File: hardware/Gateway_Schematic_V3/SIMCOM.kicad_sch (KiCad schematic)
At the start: 58 parts, among them IC2 SIM7600CE-H, J10 ANT_LTE, J11 ANT_LTE, J12 ANT_LTE, J14 SIM7100-6pin-socket-smd, Q1 MMBT3904, Q2 BC817, Q3 BC817, Q4 BC817, Q8 MMBT3904

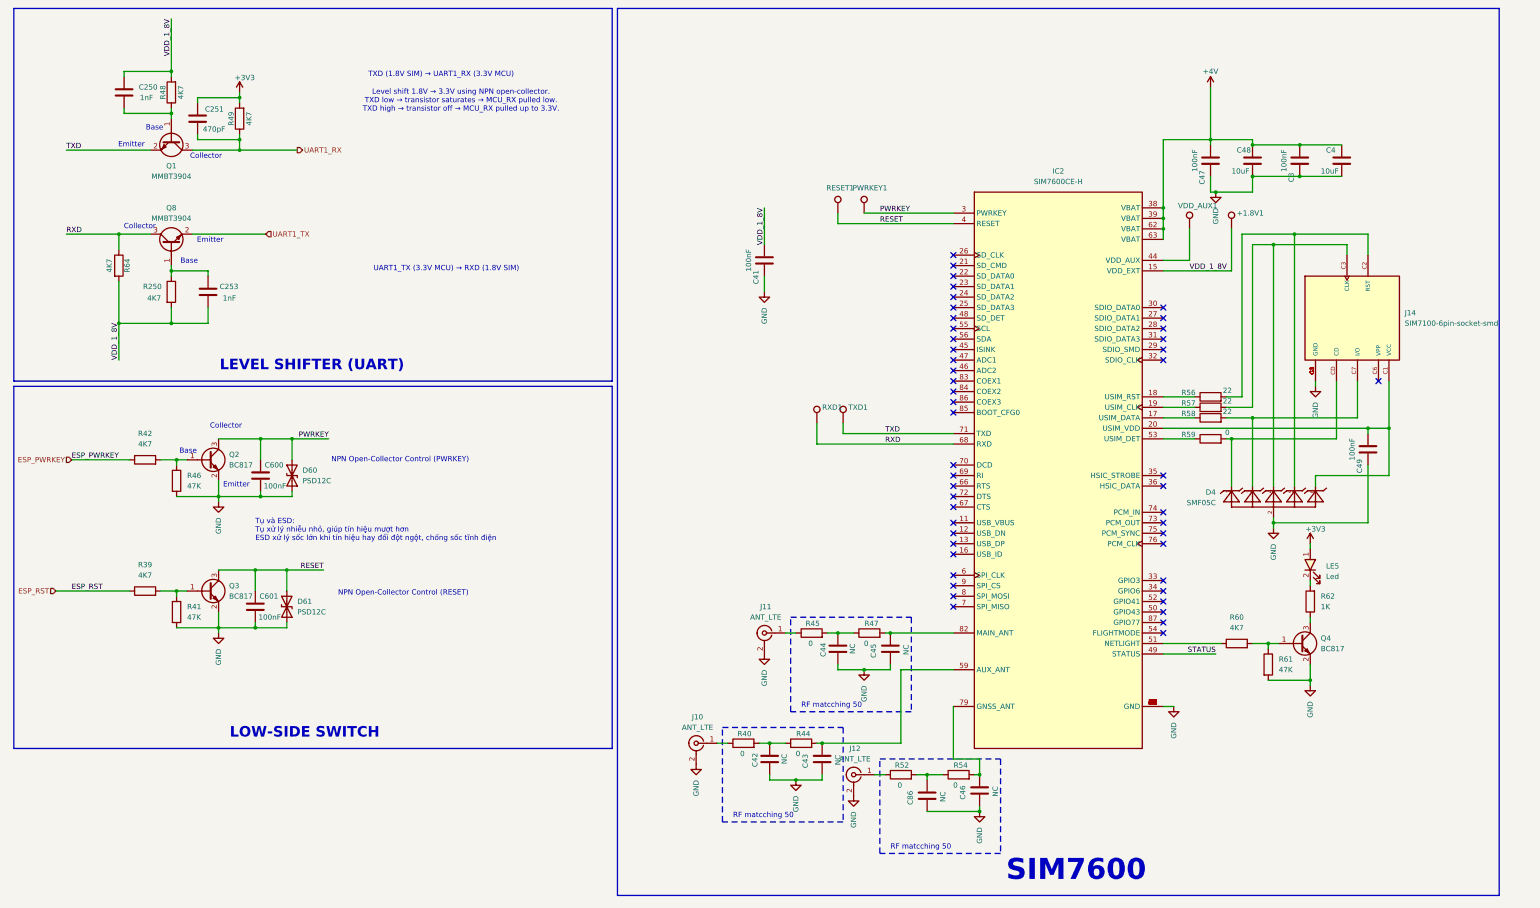
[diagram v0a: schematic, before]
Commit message: Update PCB Layout after review 27/3/2026
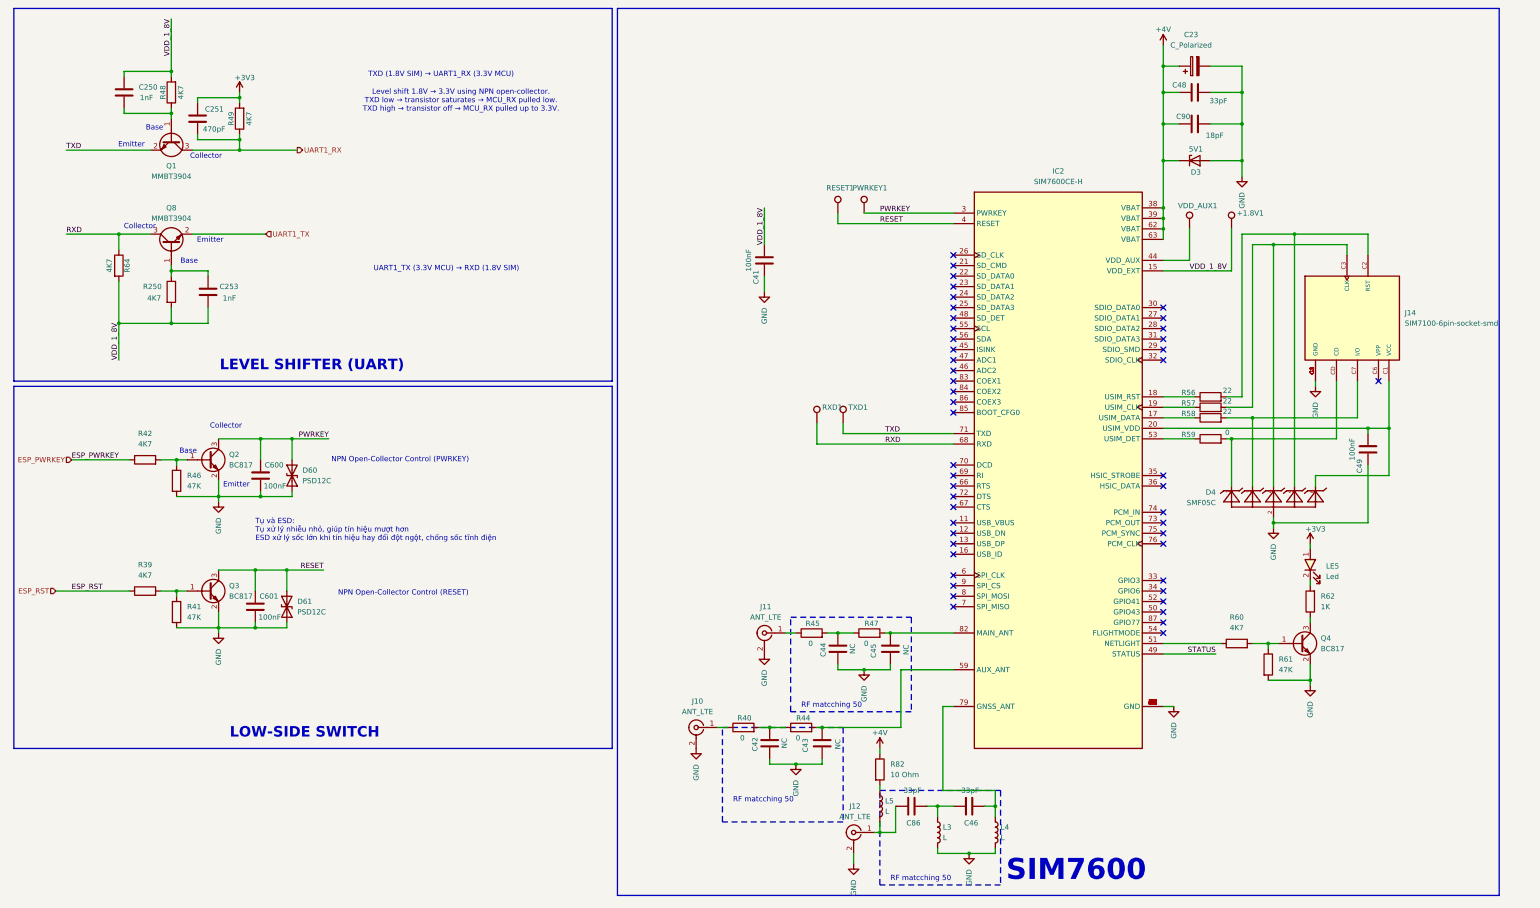
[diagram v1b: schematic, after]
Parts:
- removed C4: 10uF, Capacitor_SMD:C_0603_1608Metric, symbol Device:C
- removed C47: 100nF, Capacitor_SMD:C_0603_1608Metric, symbol Device:C
- removed R52, R54: 0, Resistor_SMD:R_0603_1608Metric, symbol Device:R
- added C23: C_Polarized, IVS_NEW_FOOTPRINT:CP_Elec_6.3x7.7, symbol Device:C_Polarized
- added D3: 5V1, IVS_NEW_FOOTPRINT:D_SOD-123, symbol Device:D_Zener
- added L3, L4, L5: L, IVS_NEW_FOOTPRINT:L_0603_1608Metric, symbol Device:L
- added R82: 10 Ohm, IVS_NEW_FOOTPRINT:R_0603_1608Metric, symbol Device:R
- C46, C86: value NC -> 33pF
- C48: value 10uF -> 33pF
- C90: renamed from C3; value 100nF -> 18pF
- J14: footprint GATEWAY_LIB:GCT_SIM7100-6-socket-smd -> IVS_NEW_FOOTPRINT:CUI_NSIM-1-A
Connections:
- net +4V: now also C23.1, D3.1 (K), R82.1
- net GND: now also C23.2, D3.2 (A), L3.2, L4.2; no longer C46.1, C86.1
- net at J12.1 (In): now also C86.2, L5.2
- net at IC2.79 (GNSS_ANT): now also C46.1, L4.1; no longer C46.2
- new net: L5.1, R82.2
- new net: C46.2, C86.1, L3.1
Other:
- moved on the sheet: C42, C43, C46, C48, C86, C90, J10, J12, R40, R44

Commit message: Update: add L_ferrite for SIMCOM
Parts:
- added L6: L_Ferrite_Small, IVS_NEW_FOOTPRINT:L_0805, symbol Device:L_Ferrite_Small
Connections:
- net +4V: now also L6.1, L6.2
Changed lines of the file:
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@@
 	(wire
 		(pts
+			(xy 293.37 40.64) (xy 294.64 40.64)
+		)
+		(stroke
+			(width 0)
+			(type default)
+		)
+	)
+	(wire
+		(pts
 			(xy 231.14 177.8) (xy 234.95 177.8)
 		)
@@
 	(wire
 		(pts
-			(xy 309.88 35.56) (xy 309.88 40.64)
+			(xy 293.37 31.75) (xy 293.37 40.64)
 		)
 		(stroke
@@
 	(wire
 		(pts
+			(xy 299.72 40.64) (xy 309.88 40.64)
+		)
+		(stroke
+			(width 0)
+			(type default)
+		)
+	)
+	(wire
+		(pts
 			(xy 341.63 81.28) (xy 341.63 142.24)
 		)
@@
 		)
 	)
+	(label "+4V"
+		(at 303.53 40.64 0)
+		(effects
+			(font
+				(size 1.27 1.27)
+			)
+			(justify left bottom)
+		)
+	)
 	(label "RESET"
 		(at 241.3 78.74 0)
@@
 	)
 	(symbol
+		(lib_id "Device:L_Ferrite_Small")
+		(at 297.18 40.64 90)
+		(unit 1)
+		(exclude_from_sim no)
+		(in_bom yes)
+		(on_board yes)
+		(dnp no)
+		(fields_autoplaced yes)
+		(property "Reference" "L6"
+			(at 297.18 34.29 90)
+			(effects
+				(font
+					(size 1.27 1.27)
+				)
+			)
+		)
+		(property "Value" "L_Ferrite_Small"
+			(at 297.18 36.83 90)
+			(effects
+				(font
+					(size 1.27 1.27)
+				)
+			)
+		)
+		(property "Footprint" "IVS_NEW_FOOTPRINT:L_0805"
+			(at 297.18 40.64 0)
+			(effects
+				(font
+					(size 1.27 1.27)
+				)
+				(hide yes)
+			)
+		)
+		(property "Datasheet" "~"
+			(at 297.18 40.64 0)
+			(effects
+				(font
+					(size 1.27 1.27)
+				)
+				(hide yes)
+			)
+		)
+		(property "Description" "Inductor with ferrite core, small symbol"
+			(at 297.18 40.64 0)
+			(effects
+				(font
+					(size 1.27 1.27)
+				)
+				(hide yes)
+			)
+		)
+		(pin "1"
+		)
+		(pin "2"
+		)
+		(instances
+			(project "Gateway_Schematic_V3"
+				(path "/08b065f5-231d-43cb-bb9e-87dca43beac9/552d244c-50bc-47f1-b1f4-fd3447251a9e"
+					(reference "L6")
+					(unit 1)
+				)
+			)
+		)
+	)
+	(symbol
 		(lib_id "Device:L")
 		(at 255.27 226.06 0)
@@
 	(symbol
 		(lib_id "power:+5V")
-		(at 309.88 35.56 0)
+		(at 293.37 31.75 0)
 		(unit 1)
 		(exclude_from_sim no)
@@
 		(dnp no)
 		(property "Reference" "#PWR074"
-			(at 309.88 39.37 0)
+			(at 293.37 35.56 0)
 			(effects
 				(font
@@
 		)
 		(property "Value" "+4V"
-			(at 309.88 31.75 0)
+			(at 293.37 27.94 0)
 			(effects
 				(font
@@
 		)
 		(property "Footprint" ""
-			(at 309.88 35.56 0)
+			(at 293.37 31.75 0)
 			(effects
 				(font
@@
 		)
 		(property "Datasheet" ""
-			(at 309.88 35.56 0)
+			(at 293.37 31.75 0)
 			(effects
 				(font
@@
 		)
 		(property "Description" "Power symbol creates a global label with name \"+5V\""
-			(at 309.88 35.56 0)
+			(at 293.37 31.75 0)
 			(effects
 				(font
